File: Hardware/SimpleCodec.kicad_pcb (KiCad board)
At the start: 4 copper layers, 59 x 95 mm, 99 parts, among them J1 RPI_ADC, J2 RP_GPIO, U1 AMS1117-5.0, U2 AMS1117-3.3, U3 MCP6002-xSN, U4 MCP6002-xSN, U5 CS4272, X1 PEDAL_COMBO_TOP

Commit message: Silkscreen and notes
Updated the board silkscreen.
Updated VCOM capacitance value.
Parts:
- added G***: LOGO, Logos:Cat, B.Cu at (170.4, 99.5)
- C37: value 10u -> 1u
- C38: value 1u -> 10u
- FB1, FB2, FB3: value 300 -> 850
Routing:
- net +5VA: track 73.3 -> 74.5 mm
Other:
- board text added: "9V 100mA"
- board text added: "DAVID MT"
- board text added: "DC"
- board text added: "IN"
- board text added: "OUT"
- board text added: "PD 04/26"
- board text added: "RP PICO 2 COMPATIBLE"
- board text added: "SIMPLE CODEC"
- board text added: "V1.0 REV A"

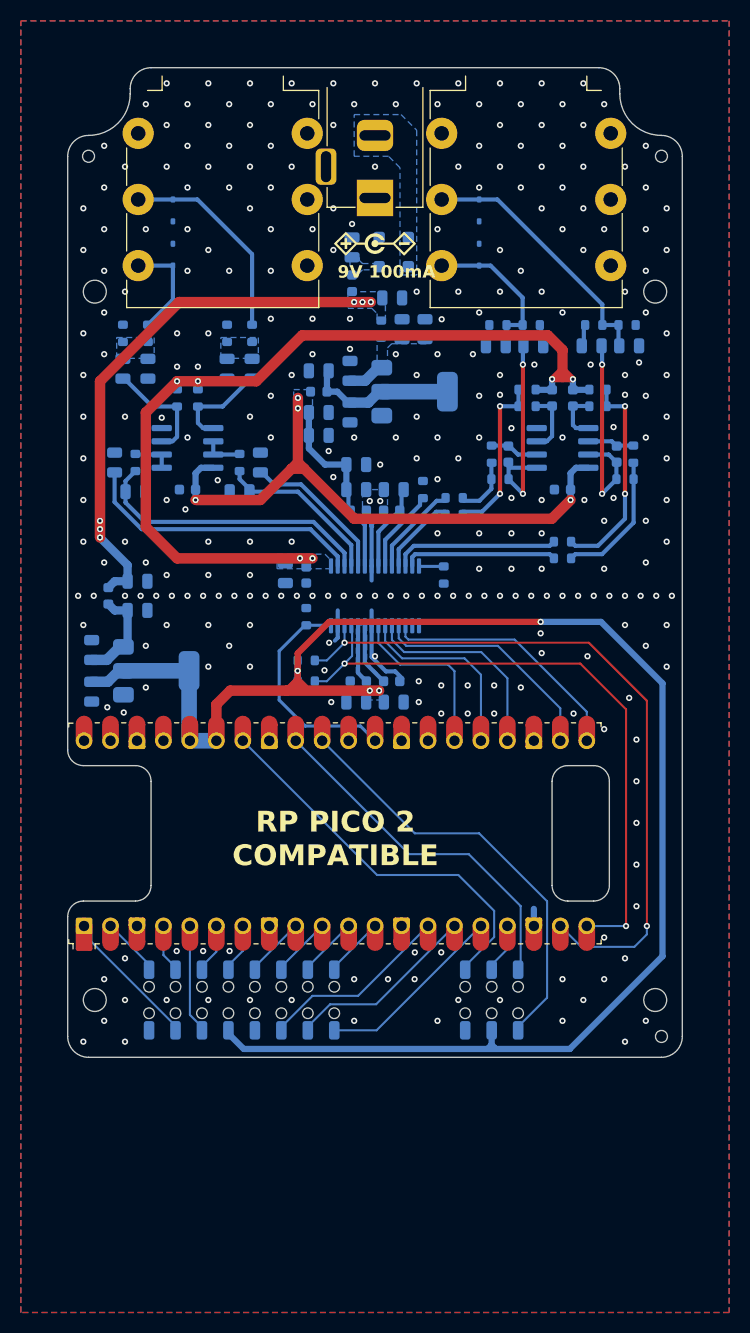
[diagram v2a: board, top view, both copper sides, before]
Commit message: Silkscreen and build
Updated the silkscreen of the PCB.
Updated all build files.
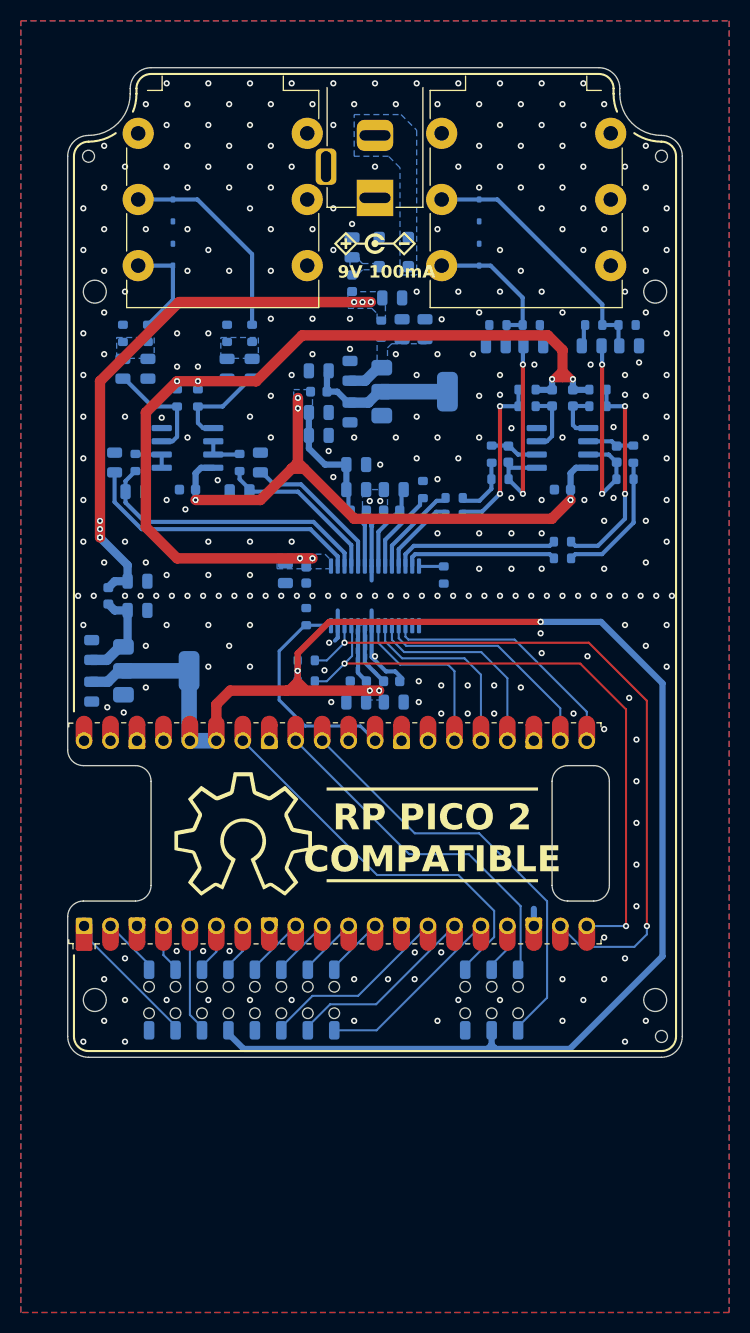
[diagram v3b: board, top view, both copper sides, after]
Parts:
- added G***: LOGO, Custom_Parts:OSHW, F.Cu at (137.3, 116.2)

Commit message: Silkscreen logos
Addedd some logos to the silkscreen layer.
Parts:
- removed the G*** at (170.4, 99.5)
- added G***: LOGO, Logos:Cat Mountain, B.Cu at (170.3, 110.5)
- added REF**: MT, Logos:MT, B.Cu at (135.4, 118.3)
- moved C1 8.40 mm to (144.8, 67.6), turned to -90 degrees
- moved C2 5.04 mm to (147.6, 67.6), turned to -90 degrees
- moved FB1 2.26 mm to (146.2, 64.8), turned to 0 degrees
- moved D1 1.46 mm to (150.4, 59.2)
- moved D2 1.41 mm to (150.4, 61.8)
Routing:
- net +VDC_PROT: track 0.00 -> 7.18 mm
- net +VCC: track 53.9 -> 59.9 mm
- net GND: vias 289 -> 288
- removed copper zone on B.Cu, net +VDC_PROT
